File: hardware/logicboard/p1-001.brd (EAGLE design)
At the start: 47 x 72 mm, 27 parts, among them IC1 74LS07N

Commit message: Silk.
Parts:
- renumbered PWR to PWR12V, VCC to VCC/VREF
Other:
- board text removed: "FRONT"
- board text removed: "IN"
- board text removed: "PWR12V"
- board text removed: "THRU"
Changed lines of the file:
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@@
 <setting verticaltext="up"/>
 </settings>
-<grid distance="1" unitdist="mm" unit="mm" style="lines" multiple="1" display="yes" altdistance="5" altunitdist="mil" altunit="mil"/>
+<grid distance="50" unitdist="mil" unit="mil" style="lines" multiple="1" display="yes" altdistance="5" altunitdist="mil" altunit="mil"/>
 <layers>
-<layer number="1" name="Top" color="4" fill="1" visible="yes" active="yes"/>
-<layer number="16" name="Bottom" color="1" fill="1" visible="yes" active="yes"/>
+<layer number="1" name="Top" color="4" fill="1" visible="no" active="yes"/>
+<layer number="16" name="Bottom" color="1" fill="1" visible="no" active="yes"/>
 <layer number="17" name="Pads" color="2" fill="1" visible="yes" active="yes"/>
 <layer number="18" name="Vias" color="2" fill="1" visible="yes" active="yes"/>
@@
 <hole x="44" y="69" drill="3.2"/>
 <hole x="3" y="69" drill="3.2"/>
-<text x="14" y="62" size="0.8128" layer="25" rot="R90" align="center">FRONT</text>
-<text x="7" y="12" size="0.8128" layer="25" rot="R90" align="center">PWR12V</text>
-<text x="41" y="21" size="0.8128" layer="25" rot="R90" align="center-left">THRU</text>
-<text x="41" y="5" size="0.8128" layer="25" rot="R90" align="center-right">IN</text>
 <text x="3.81" y="55.88" size="1.016" layer="25" rot="R90">Pineapple I 1.0.0
 Pineapple Design</text>
@@
 <text x="40.64" y="43.18" size="0.8128" layer="25" rot="R90" align="center">D7</text>
 <text x="40.64" y="33.02" size="0.8128" layer="25" rot="R90" align="center">I2C</text>
-<text x="44.91" y="23.02" size="0.8128" layer="25" rot="R90" align="bottom-right">I2C</text>
 <hole x="17.78" y="8.89" drill="1"/>
 <hole x="33.02" y="8.89" drill="1"/>
@@
 </element>
 <element name="FRONT" library="SparkFun-Connectors" package="JST-4-PTH" value="" x="21" y="62" smashed="yes" rot="R90">
-<attribute name="NAME" x="16" y="62" size="0.6096" layer="25" font="vector" ratio="20" rot="R90" align="center"/>
+<attribute name="NAME" x="14" y="62" size="0.8128" layer="25" font="vector" ratio="20" rot="R90" align="center"/>
 <attribute name="PROD_ID" value="WIRE-13531" x="21" y="62" size="1.778" layer="27" rot="R90" display="off"/>
 <attribute name="SF_ID" value="PRT-09916" x="21" y="62" size="1.778" layer="27" rot="R90" display="off"/>
@@
 <attribute name="VALUE" x="40.005" y="62.611" size="1.27" layer="27" ratio="10" rot="R270"/>
 </element>
-<element name="PWR" library="SparkFun-Connectors" package="JST-2-PTH" value="12V" x="14" y="12" smashed="yes" rot="R90">
-<attribute name="NAME" x="9" y="12" size="0.6096" layer="25" font="vector" ratio="20" rot="R90" align="center"/>
+<element name="PWR12V" library="SparkFun-Connectors" package="JST-2-PTH" value="12V" x="14" y="12" smashed="yes" rot="R90">
+<attribute name="NAME" x="7" y="12" size="0.8128" layer="25" font="vector" ratio="20" rot="R90" align="center"/>
 <attribute name="PROD_ID" value="CONN-09863" x="14" y="12" size="1.778" layer="27" rot="R90" display="off"/>
 <attribute name="SKU" value="PRT-09914" x="14" y="12" size="1.778" layer="27" rot="R90" display="off"/>
@@
 </element>
 <element name="THRU" library="SparkFun-Connectors" package="JST-3-PTH" value="" x="41" y="16" smashed="yes" rot="R270">
-<attribute name="NAME" x="46" y="16" size="0.6096" layer="25" font="vector" ratio="20" rot="R270" align="center"/>
+<attribute name="NAME" x="39" y="16" size="0.8128" layer="25" font="vector" ratio="20" rot="R270" align="center"/>
 <attribute name="PROD_ID" value="WIRE-10037" x="41" y="16" size="1.778" layer="27" rot="R270" display="off"/>
 <attribute name="SF_ID" value="PRT-09915" x="41" y="16" size="1.778" layer="27" rot="R270" display="off"/>
@@
 </element>
 <element name="IN" library="SparkFun-Connectors" package="JST-2-PTH" value="" x="41" y="9" smashed="yes" rot="R270">
-<attribute name="NAME" x="46" y="9" size="0.6096" layer="25" font="vector" ratio="20" rot="R270" align="center"/>
+<attribute name="NAME" x="39" y="9" size="0.8128" layer="25" font="vector" ratio="20" rot="R270" align="center"/>
 <attribute name="PROD_ID" value="CONN-09863" x="41" y="9" size="1.778" layer="27" rot="R270" display="off"/>
 <attribute name="SKU" value="PRT-09914" x="41" y="9" size="1.778" layer="27" rot="R270" display="off"/>
@@
 </element>
 <element name="I2C" library="SparkFun-Connectors" library_urn="urn:adsk.eagle:library:513" package="1X05_1MM_RA" package3d_urn="urn:adsk.eagle:package:38106/1" value="" x="41" y="28" smashed="yes" rot="R90">
-<attribute name="NAME" x="44" y="28" size="0.6096" layer="25" font="vector" ratio="20" rot="R90" align="center"/>
+<attribute name="NAME" x="46" y="28" size="0.6096" layer="25" font="vector" ratio="20" rot="R90" align="center"/>
 <attribute name="VALUE" x="44.302" y="26.349" size="0.6096" layer="27" font="vector" ratio="20" rot="R90"/>
 </element>
@@
 <attribute name="VALUE" x="40.005" y="34.29" size="1.27" layer="27" rot="R90"/>
 </element>
-<element name="VCC" library="SparkFun-Connectors" library_urn="urn:adsk.eagle:library:513" package="JST-3-PTH-VERT" package3d_urn="urn:adsk.eagle:package:38080/1" value="" x="4" y="12" smashed="yes" rot="R90">
+<element name="VCC/VREF" library="SparkFun-Connectors" library_urn="urn:adsk.eagle:library:513" package="JST-3-PTH-VERT" package3d_urn="urn:adsk.eagle:package:38080/1" value="" x="4" y="12" smashed="yes" rot="R90">
 <attribute name="NAME" x="1" y="12" size="0.8128" layer="25" font="vector" ratio="20" rot="R90" align="center"/>
 <attribute name="PROD_ID" value="CONN-13230" x="4" y="12" size="1.778" layer="27" rot="R90" display="off"/>
@@
 <contactref element="U$1" pad="P$21"/>
 <contactref element="CH" pad="C"/>
-<contactref element="PWR" pad="2"/>
+<contactref element="PWR12V" pad="2"/>
 <contactref element="IC1" pad="3"/>
 <contactref element="IC1" pad="5"/>
@@
 <contactref element="I2C" pad="5"/>
 <contactref element="VOUT" pad="3"/>
-<contactref element="VCC" pad="2"/>
+<contactref element="VCC/VREF" pad="2"/>
 <wire x1="10.922" y1="28.194" x2="10.922" y2="33.274" width="0.254" layer="1"/>
 <wire x1="10.922" y1="33.274" x2="11" y2="33.46" width="0.254" layer="1"/>
@@
 <contactref element="R2" pad="1"/>
 <contactref element="I2C" pad="1"/>
-<contactref element="VCC" pad="1"/>
+<contactref element="VCC/VREF" pad="1"/>
 <wire x1="29.21" y1="48.768" x2="29.21" y2="48.26" width="0.254" layer="1"/>
 <wire x1="25.654" y1="52.324" x2="29.21" y2="48.768" width="0.254" layer="1"/>
@@
 <contactref element="U$1" pad="P$20"/>
 <contactref element="C1" pad="1"/>
-<contactref element="PWR" pad="1"/>
+<contactref element="PWR12V" pad="1"/>
 <wire x1="15.24" y1="9.906" x2="15.24" y2="6.35" width="0.254" layer="1"/>
 <wire x1="14.224" y1="10.922" x2="15.24" y2="9.906" width="0.254" layer="1"/>
@@
 <signal name="VREF">
 <contactref element="U$1" pad="P$32"/>
-<contactref element="VCC" pad="3"/>
+<contactref element="VCC/VREF" pad="3"/>
 <wire x1="4.318" y1="13.462" x2="4.318" y2="13.97" width="0.254" layer="16"/>
 <wire x1="3.302" y1="12.446" x2="4.318" y2="13.462" width="0.254" layer="16"/>

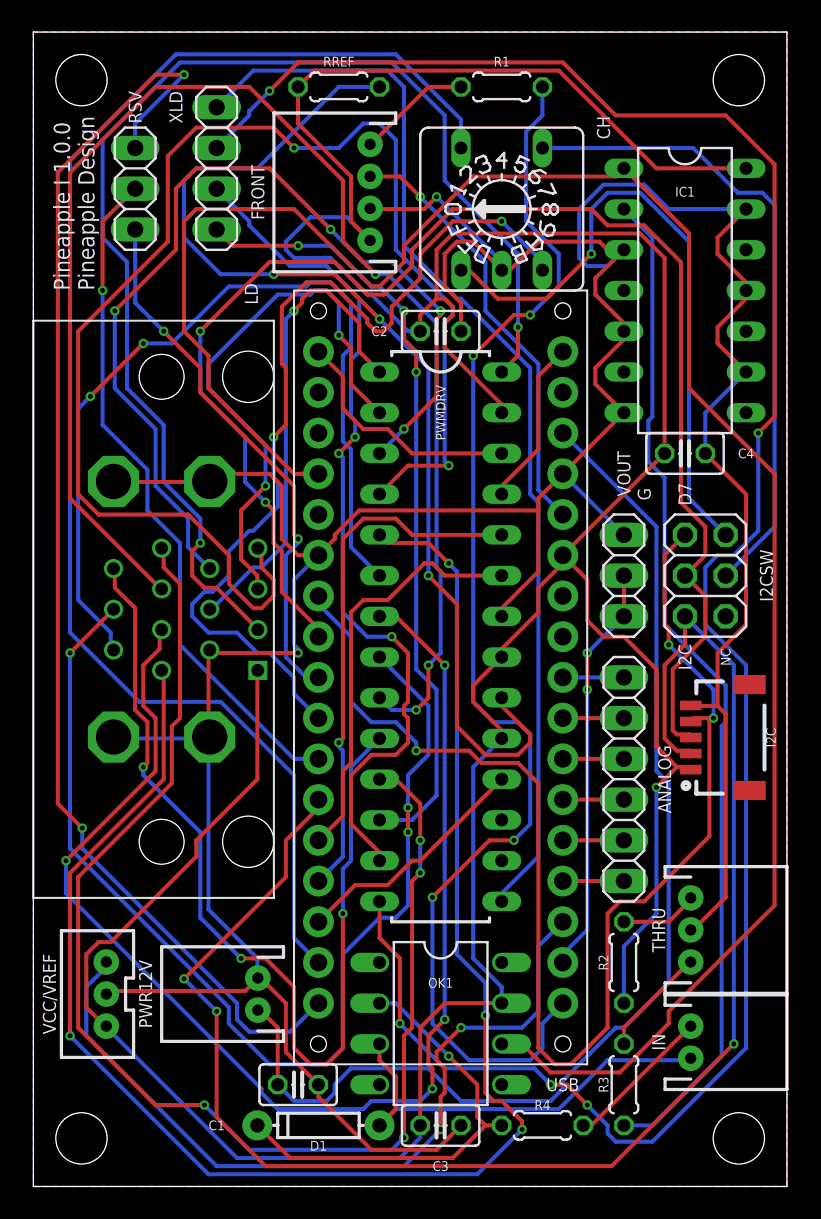
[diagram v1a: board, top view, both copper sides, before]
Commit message: I2C pull-up.
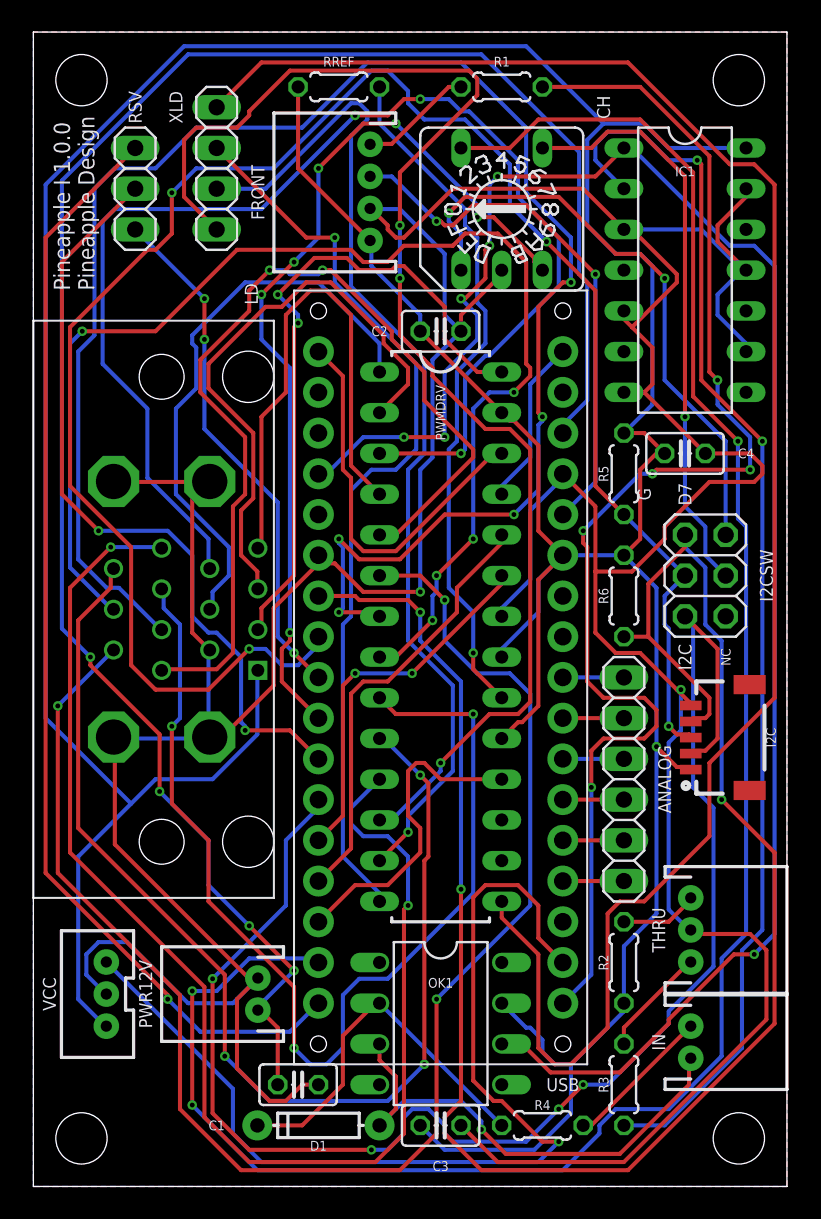
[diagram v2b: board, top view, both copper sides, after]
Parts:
- removed VOUT: (no value), pinhead:1X03
- added R5, R6: 5.6k, resistor:0204/5
- moved IC1 1.27 mm to (40.6, 57.1)
- renumbered VCC/VREF to VCC
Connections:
- removed net 3V: U$1.P$33, VOUT.1, VOUT.2
- removed net VREF: U$1.P$32, VCC.3
- new net V3V: U$1.P$33, VCC.3
- net GND: no longer VOUT.3
- net SCL: now also R5.1
- net SDA: now also R6.1
- net VCC: now also R5.2, R6.2
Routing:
- net LD15: track 133.8 -> 56.9 mm, vias 5 -> 1
- net V3V: track 0.00 -> 63.0 mm, vias 0 -> 1
- net LD5: track 87.0 -> 32.6 mm, vias 2 -> 0
- net GND: track 238.0 -> 292.0 mm
- net VREF: track 50.4 -> 0.00 mm, vias 2 -> 0
- net VDD: track 72.4 -> 120.3 mm, vias 0 -> 4
- net LD16: track 68.4 -> 112.7 mm
- net LD6: track 100.7 -> 59.2 mm, vias 4 -> 2
- net LD7: track 55.0 -> 95.5 mm, vias 2 -> 3
- net SW8: track 90.0 -> 127.6 mm, vias 0 -> 3
- net LD1: track 78.4 -> 41.8 mm
- net LD13: track 49.0 -> 84.7 mm
- net SDA: track 81.6 -> 115.5 mm
- net VCC: track 241.6 -> 273.4 mm
- net LD8: track 80.9 -> 109.7 mm, vias 4 -> 5
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
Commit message: Layout.
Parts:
- removed ANALOG: (no value), pinhead:1X06
- removed CH: (no value), switch-dil:A1353HEX
- removed I2CSW: (no value), pinhead:2X03
- removed XLD: (no value), pinhead:1X04
- RSV: device pinhead:1X03 -> pinhead:1X05
- moved RSV 60.7 mm to (43.2, 14.0)
- moved R3 42.4 mm to (43.2, 48.3)
- moved R2 34.5 mm to (40.6, 48.3)
- moved D1 28.7 mm to (38.1, 24.1), turned to 90 degrees
- moved I2C 25.3 mm to (27.9, 6.35), turned to 0 degrees
- moved IN 24.0 mm to (41.0, 33.0)
- moved THRU 24.0 mm to (41.0, 40.0)
- moved R4 23.3 mm to (40.6, 25.4), turned to 90 degrees
- moved R5 20.1 mm to (43.2, 25.4)
- moved R6 14.5 mm to (45.7, 25.4)
- moved C2 14.0 mm to (24.1, 67.3)
- moved VCC 13.6 mm to (15.0, 4.00), turned to 0 degrees
- moved RREF 11.5 mm to (30.5, 67.3)
- moved C3 9.25 mm to (34.3, 6.35)
- moved R1 8.98 mm to (38.1, 67.3)
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- renumbered LD to LIGHTDRIVE
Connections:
- net RSV1 renamed N$1
- removed net AI1: ANALOG.1, U$1.P$31
- removed net AI2: ANALOG.2, U$1.P$30
- removed net AI3: ANALOG.3, U$1.P$29
- removed net AI4: ANALOG.4, U$1.P$28
- removed net AI5: ANALOG.5, U$1.P$27
- removed net AI6: ANALOG.6, U$1.P$26
- removed net LD13: PWMDRV.12, XLD.1
- removed net LD14: PWMDRV.13, XLD.2
- removed net LD15: PWMDRV.14, XLD.3
- removed net LD16: PWMDRV.15, XLD.4
- removed net RSV2: RSV.2, U$1.P$7
- removed net RSV3: RSV.3, U$1.P$1
- removed net SW1: CH.1, I2CSW.2
- removed net SW2: CH.2, I2CSW.4
- removed net SW4: CH.4, U$1.P$8
- removed net SW8: CH.8, U$1.P$2
- new net N$4: RSV.2, U$1.P$8
- new net N$6: RSV.3, U$1.P$7
- new net N$7: RSV.4, U$1.P$2
- new net N$8: RSV.5, U$1.P$1
- net D7: no longer I2CSW.5
- net GND: no longer CH.C
- net SCL: no longer I2CSW.3
- net SDA: no longer I2CSW.1
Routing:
- net GND: track 292.0 -> 0.00 mm, vias 2 -> 0
- net VCC: track 273.4 -> 0.00 mm, vias 1 -> 0
- net SW8: track 127.6 -> 0.00 mm, vias 3 -> 0
- net VDD: track 120.3 -> 0.00 mm, vias 4 -> 0
- net SCL: track 117.8 -> 0.00 mm, vias 4 -> 0
- net SDA: track 115.5 -> 0.00 mm, vias 3 -> 0
- net LD16: track 112.7 -> 0.00 mm
- net RX: track 111.6 -> 0.00 mm, vias 6 -> 0
- net LD8: track 109.7 -> 0.00 mm, vias 5 -> 0
- net LD7: track 95.5 -> 0.00 mm, vias 3 -> 0
- net D7: track 95.4 -> 0.00 mm, vias 4 -> 0
- net LD13: track 84.7 -> 0.00 mm, vias 3 -> 0
- net LD12: track 82.9 -> 0.00 mm, vias 2 -> 0
- net LD4: track 82.2 -> 0.00 mm, vias 3 -> 0
- net IND: track 81.6 -> 0.00 mm, vias 5 -> 0
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- removed copper zone on layer 1, net GND
- removed copper zone on layer 16, net GND
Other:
- board text added: "/"
- board text added: "Pineapple / 1.0.0 Pineapple Design"
- board text removed: "D7"
- board text removed: "G"
- board text removed: "I2C"
- board text removed: "NC"
- board text removed: "Pineapple I 1.0.0 Pineapple Design"

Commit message: New layout.
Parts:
- removed C4: 103, rcl:C025-025X050
- RREF: device resistor:0204/5 -> pinhead:1X02
- RSV: device pinhead:1X05 -> SparkFun-Connectors:JST-5-PTH-VERT
- VCC: device SparkFun-Connectors:JST-3-PTH-VERT -> SparkFun-Connectors:JST-3-PTH
- moved RREF 53.9 mm to (44.5, 15.2), turned to 90 degrees
- moved R1 42.0 mm to (40.6, 25.4), turned to 90 degrees
- moved RSV 40.2 mm to (3.00, 12.0)
- moved C2 23.4 mm to (43.4, 54.0)
- moved R4 23.4 mm to (45.7, 48.3)
- moved D1 9.25 mm to (40.6, 15.2)
- moved VCC 3.61 mm to (17.0, 7.00), turned to 90 degrees
- moved PWR12V 3.00 mm to (17.0, 14.0)
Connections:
- net GND: no longer C4.2
- net VCC: no longer C4.1
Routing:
- net VCC: track 0.00 -> 230.6 mm
- net GND: track 0.00 -> 204.5 mm, vias 0 -> 1
- net SDA: track 0.00 -> 161.0 mm, vias 0 -> 4
- net LD11: track 0.00 -> 102.2 mm, vias 0 -> 5
- net LD7: track 0.00 -> 97.3 mm, vias 0 -> 5
- net LD9: track 0.00 -> 75.7 mm, vias 0 -> 4
- net LD8: track 0.00 -> 72.7 mm, vias 0 -> 4
- net D7: track 0.00 -> 67.7 mm
- net SCL: track 0.00 -> 63.3 mm, vias 0 -> 1
- net LD10: track 0.00 -> 62.8 mm, vias 0 -> 3
- net RX: track 0.00 -> 62.2 mm, vias 0 -> 1
- net N$5: track 0.00 -> 59.6 mm
- net LD3: track 0.00 -> 57.3 mm, vias 0 -> 1
- net VDD: track 0.00 -> 56.7 mm, vias 0 -> 3
- net IREF: track 0.00 -> 55.5 mm
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- added copper zone on layer 1, net GND
- added copper zone on layer 16, net GND

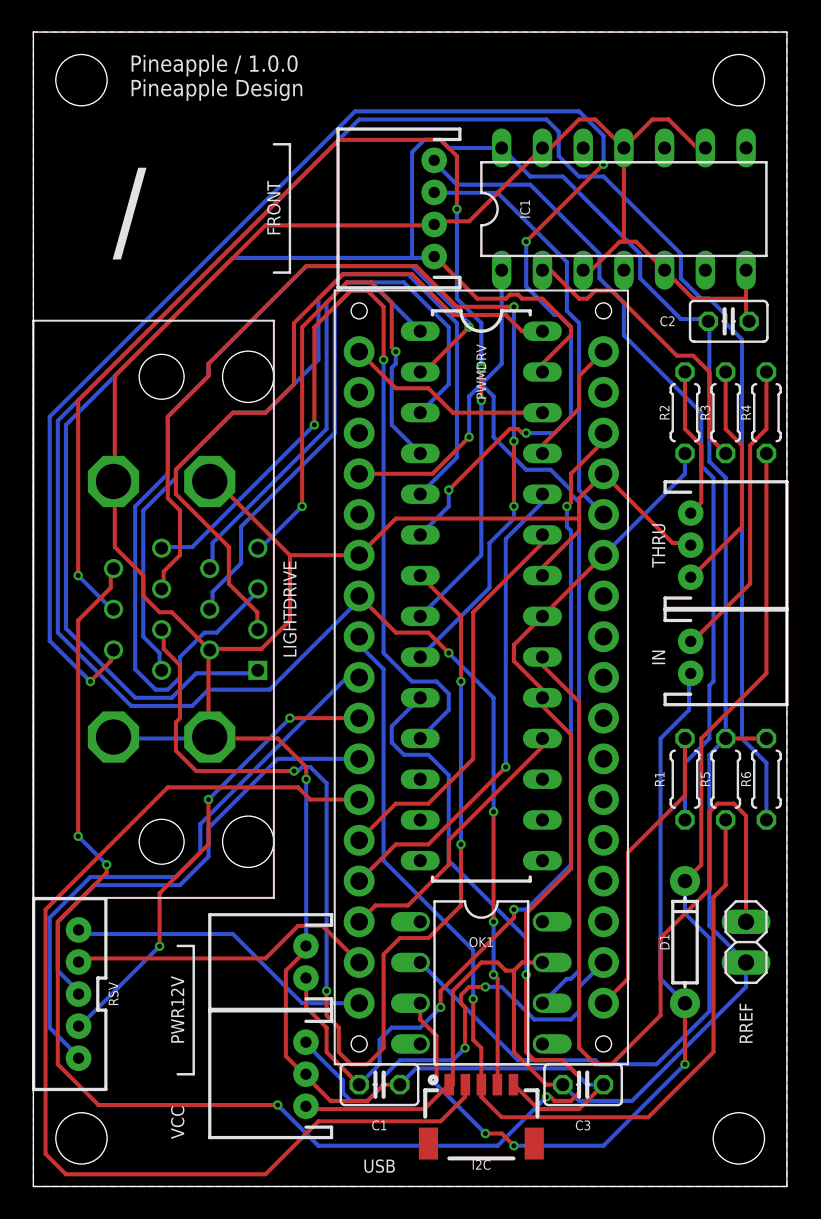
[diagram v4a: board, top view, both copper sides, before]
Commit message: New analog/reserve ports.
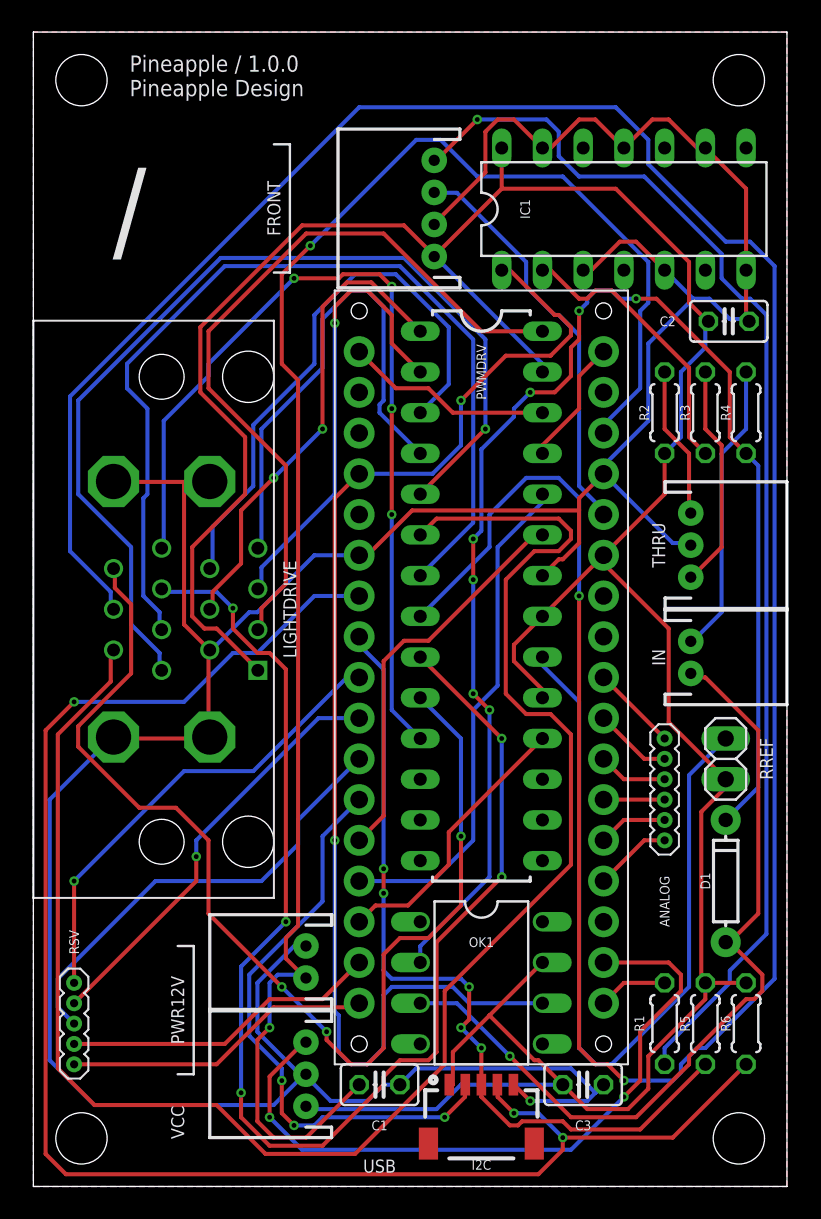
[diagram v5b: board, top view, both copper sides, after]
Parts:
- added ANALOG: (no value), SparkFun-Connectors:1X06_1.27MM
- RSV: device SparkFun-Connectors:JST-5-PTH-VERT -> SparkFun-Connectors:1X05_1.27MM
- moved R1 15.3 mm to (39.4, 10.2)
- moved R5 15.3 mm to (41.9, 10.2)
- moved R6 15.3 mm to (44.5, 10.2)
- moved RREF 11.5 mm to (43.2, 26.7)
- moved D1 4.58 mm to (43.2, 19.1)
- moved R2 1.27 mm to (39.4, 48.3)
- moved R3 1.27 mm to (41.9, 48.3)
- moved R4 1.27 mm to (44.5, 48.3)
- moved RSV 0.84 mm to (2.54, 12.7), turned to 270 degrees
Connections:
- net N$1 renamed D4
- net N$4 renamed D5
- net N$6 renamed D6
- net N$7 renamed D11
- net N$8 renamed D12
- new net N$10: ANALOG.2, U$1.P$30
- new net N$11: ANALOG.3, U$1.P$29
- new net N$12: ANALOG.4, U$1.P$28
- new net N$13: ANALOG.5, U$1.P$27
- new net N$14: ANALOG.6, U$1.P$26
- new net N$9: ANALOG.1, U$1.P$31
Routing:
- net LD9: track 75.7 -> 180.8 mm, vias 4 -> 2
- net SDA: track 161.0 -> 102.8 mm, vias 4 -> 3
- net VDD: track 56.7 -> 106.1 mm, vias 3 -> 2
- net VCC: track 230.6 -> 190.9 mm
- net LD11: track 102.2 -> 69.5 mm, vias 5 -> 3
- net D7: track 67.7 -> 36.5 mm, vias 0 -> 3
- net LD3: track 57.3 -> 28.6 mm
- net N$5: track 59.6 -> 88.2 mm, vias 0 -> 7
- net N$3: track 51.7 -> 78.0 mm, vias 0 -> 1
- net LD10: track 62.8 -> 83.8 mm, vias 3 -> 5
- net RX: track 62.2 -> 78.9 mm, vias 1 -> 2
- net V3V: track 29.3 -> 44.2 mm
- net IND: track 18.6 -> 4.34 mm
- net LD8: track 72.7 -> 59.8 mm, vias 4 -> 0
- net SCL: track 63.3 -> 51.5 mm, vias 1 -> 5
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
